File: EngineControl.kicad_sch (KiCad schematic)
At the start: 0 parts

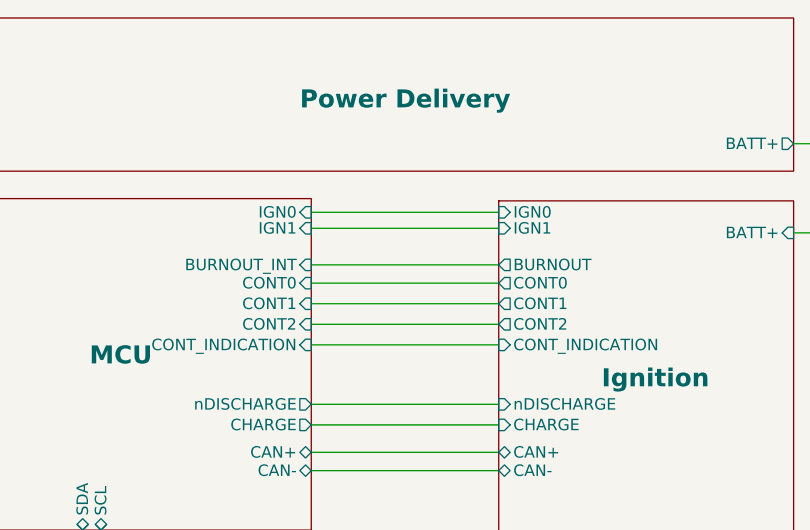
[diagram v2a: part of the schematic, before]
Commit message: #1 Make connections for IGN2
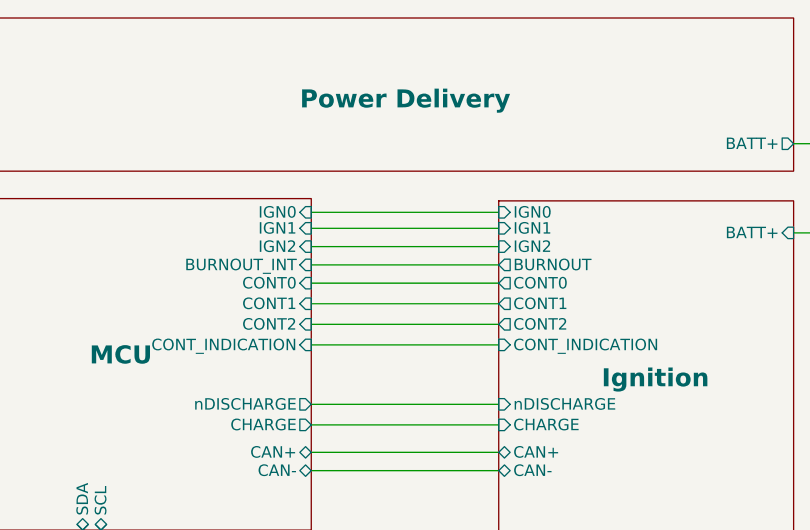
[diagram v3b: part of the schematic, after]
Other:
- sheet Ignition ports: added IGN2; removed none
- sheet MCU ports: added IGN2; removed none
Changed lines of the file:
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@@
+    (stroke (width 0) (type solid) (color 0 0 0 0))
+  )
+  (wire (pts (xy 142.24 59.944) (xy 163.068 59.944))
     (stroke (width 0) (type solid) (color 0 0 0 0))
   )
@@
       (effects (font (size 1.27 1.27)) (justify left))
     )
+    (pin "IGN2" input (at 163.068 59.944 180)
+      (effects (font (size 1.27 1.27)) (justify left))
+    )
   )
   (sheet (at 102.108 54.61) (size 40.132 36.83)
@@
       (effects (font (size 1.27 1.27)) (justify right))
     )
+    (pin "IGN2" input (at 142.24 59.944 0)
+      (effects (font (size 1.27 1.27)) (justify right))
+    )
